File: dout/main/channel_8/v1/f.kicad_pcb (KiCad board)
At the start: 2 copper layers, 76.8 x 81.3 mm, 13 parts, among them J1 fm16_i, J10 data_manager_i, J11 wrs_i, J12 selector4_i, J13 bus_i, J2 dio_channel_i, J3 dio_channel_i, J4 dio_channel_i, J5 dio_channel_i, J6 dio_channel_i, J7 dio_channel_i, J8 dio_channel_i, J9 dio_channel_i

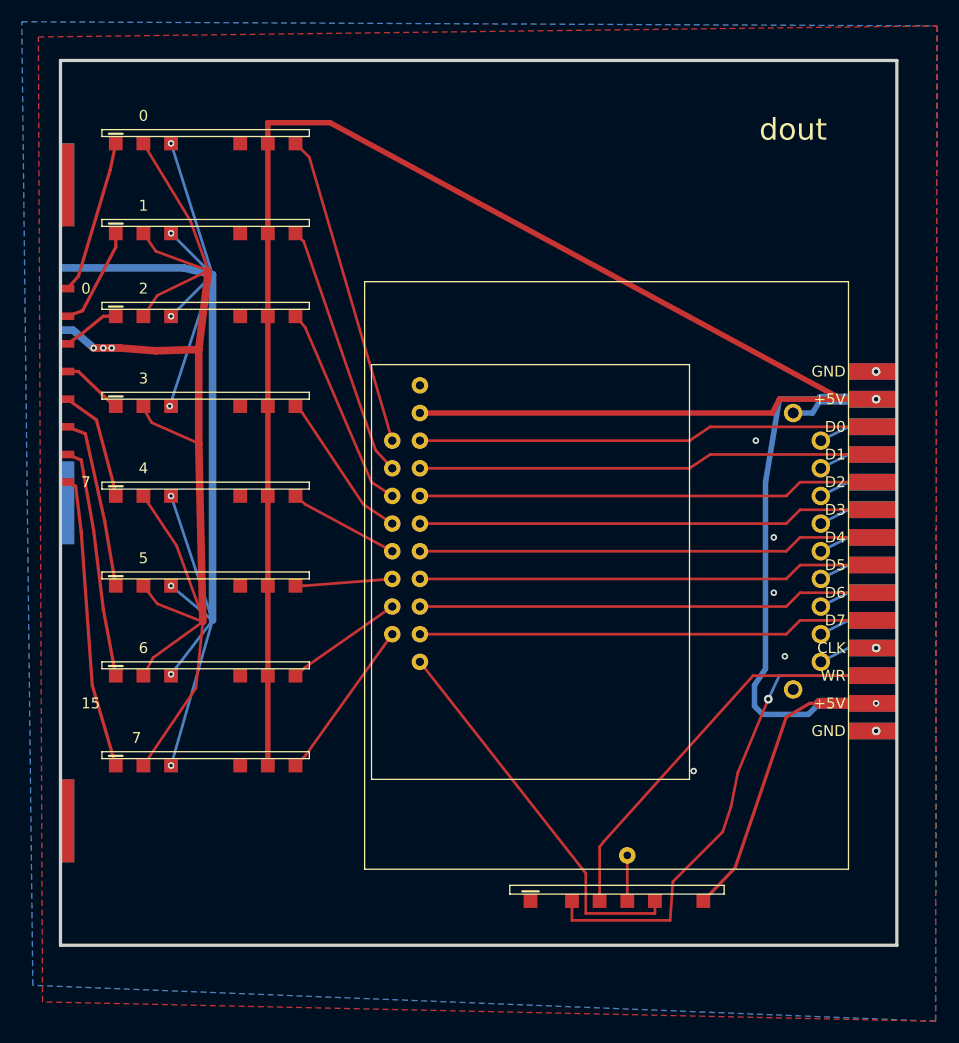
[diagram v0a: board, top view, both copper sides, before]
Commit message: voltage regulator for each module
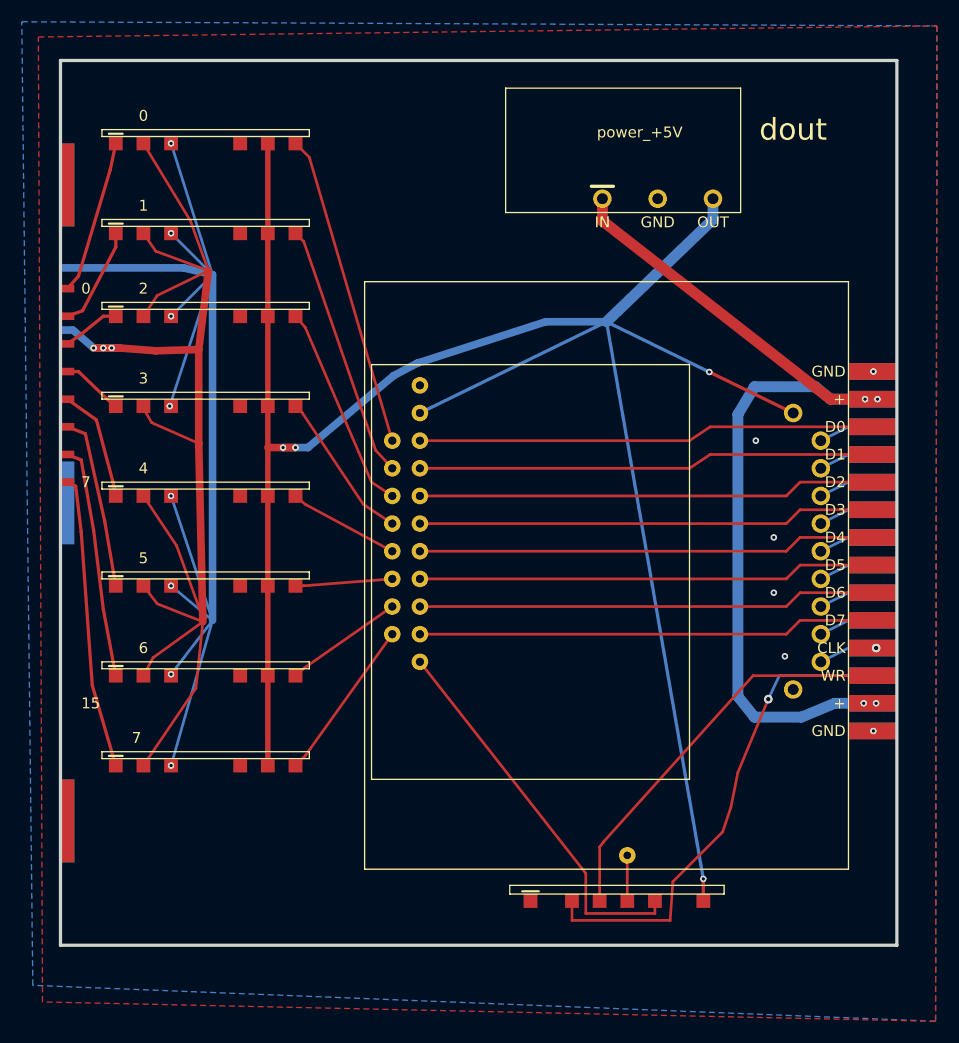
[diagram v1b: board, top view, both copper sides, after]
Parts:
- added J14: power_+5V, plc88:power_i, F.Cu at (-1.02, -3.81)
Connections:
- J13 pad 25: +5V -> VPBUS
- J13 pad 26: +5V -> VPBUS
- J13 pad 3: +5V -> VPBUS
- J13 pad 4: +5V -> VPBUS
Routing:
- net VPBUS: track 0.00 -> 86.4 mm, vias 0 -> 4
- net +5V: track 240.7 -> 200.3 mm, vias 2 -> 4
- net GND: vias 7 -> 6
